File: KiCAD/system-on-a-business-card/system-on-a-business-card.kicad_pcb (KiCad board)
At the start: 2 copper layers, 85 x 54 mm, 92 parts, among them J1 USB_C_Receptacle, J2 X077-6428TSWCG01-H13, J3 Conn_01x04_Socket, J4 TF-018B-H15, Q1 2N7002K, Q2 2N7002K, SW1 SW_Push, SW2 SW_Push, U1 USBLC6-2SC6, U2 ESP32-C3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

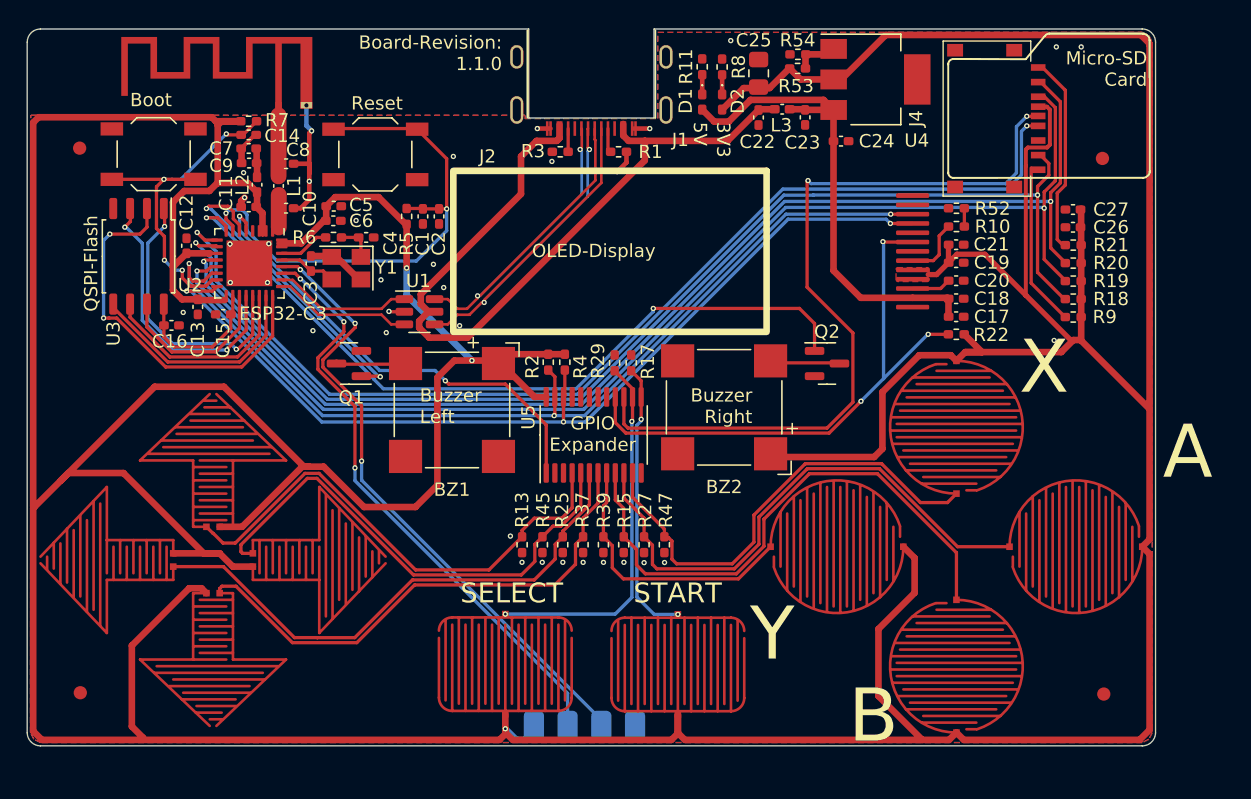
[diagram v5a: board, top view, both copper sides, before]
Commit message: #10: created version with DAC, Op Amp and speaker
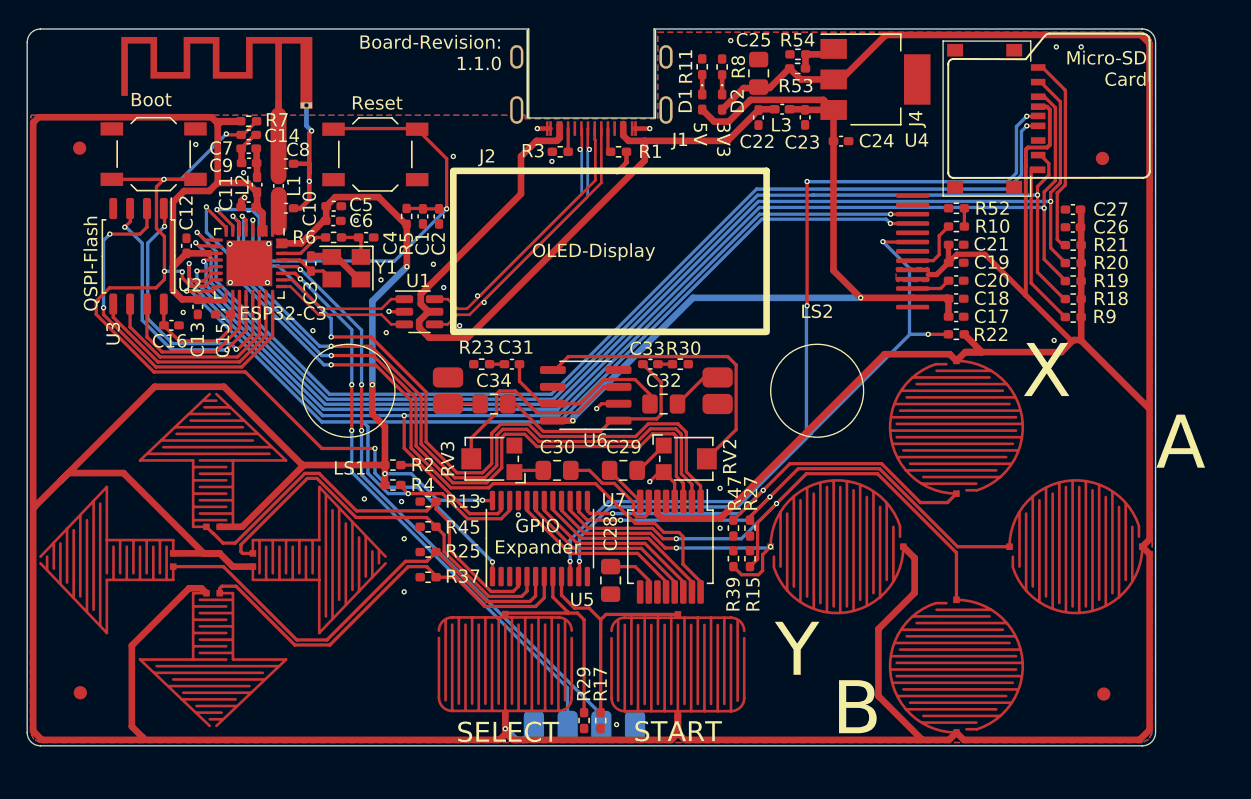
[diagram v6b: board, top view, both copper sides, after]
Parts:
- removed BZ1, BZ2: MLT-7525, Buzzer_Beeper:MagneticBuzzer_CUI_CMT-8504-100-SMT
- removed Q1, Q2: 2N7002K, Package_TO_SOT_SMD:SOT-23
- added C28: 10u, Capacitor_SMD:C_0805_2012Metric_Pad1.18x1.45mm_HandSolder, F.Cu at (121.5, 111.5)
- added C29: 10u, Capacitor_SMD:C_0805_2012Metric_Pad1.18x1.45mm_HandSolder, F.Cu at (122.4, 103.2)
- added C30: 10u, Capacitor_SMD:C_0805_2012Metric_Pad1.18x1.45mm_HandSolder, F.Cu at (117.4, 103.2)
- added C31: 50n, Capacitor_SMD:C_0402_1005Metric_Pad0.74x0.62mm_HandSolder, F.Cu at (114.0, 95.2)
- added C32: 250u, Capacitor_SMD:C_0805_2012Metric_Pad1.18x1.45mm_HandSolder, F.Cu at (125.5, 98.2)
- added C33: 50n, Capacitor_SMD:C_0402_1005Metric_Pad0.74x0.62mm_HandSolder, F.Cu at (124.5, 95.2)
- added C34: 250u, Capacitor_SMD:C_0805_2012Metric_Pad1.18x1.45mm_HandSolder, F.Cu at (112.7, 98.2)
- added LS1: Speaker_Left, Prj_speaker:Radial_10mm, F.Cu at (101.7, 97.2)
- added LS2: Speaker_Right, Prj_speaker:Radial_10mm, F.Cu at (137.0, 97.2)
- added R23: 10R, Resistor_SMD:R_0402_1005Metric_Pad0.72x0.64mm_HandSolder, F.Cu at (111.7, 95.2)
- added R30: 10R, Resistor_SMD:R_0402_1005Metric_Pad0.72x0.64mm_HandSolder, F.Cu at (126.7, 95.2)
- added RV2: 10k, Potentiometer_SMD:Potentiometer_Bourns_TC33X_Vertical, F.Cu at (127.2, 102.4)
- added RV3: 10k, Potentiometer_SMD:Potentiometer_Bourns_TC33X_Vertical, F.Cu at (112.4, 102.4)
- added U6: RC4580, Package_SO:SOIC-8_3.9x4.9mm_P1.27mm, F.Cu at (119.6, 97.6)
- added U7: PCM1754, Package_SO:SSOP-16_5.3x6.2mm_P0.65mm, F.Cu at (126.0, 109.0)
- moved R17 27.0 mm to (120.7, 122.1), turned to -90 degrees
- moved R29 27.0 mm to (119.5, 122.1), turned to -90 degrees
- moved R4 15.9 mm to (105.0, 104.3), turned to 0 degrees
- moved R2 14.0 mm to (105.0, 102.8), turned to 0 degrees
- moved R37 11.9 mm to (107.7, 111.3), turned to 180 degrees
- moved R25 10.2 mm to (107.7, 109.4), turned to 180 degrees
- moved R39 9.85 mm to (130.7, 109.9), turned to 90 degrees
- moved R15 9.57 mm to (131.9, 109.9), turned to 90 degrees
- moved U5 8.79 mm to (116.1, 108.4)
- moved R45 8.72 mm to (107.7, 107.5), turned to 180 degrees
- moved R27 8.08 mm to (131.9, 107.6)
- moved R13 7.79 mm to (107.7, 105.6), turned to 180 degrees
- moved R47 5.35 mm to (130.7, 107.6)
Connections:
- U2 pad 4: unconnected-(U2-XTAL_32K_P/ADC1_CH0-Pad4) -> /Audio Circuit/BCLK
- U2 pad 5: /Host/IO_EXP_INT -> /Audio Circuit/SERIAL_DATA
- U2 pad 6: BUZZER_L -> /Audio Circuit/LRCLK
- U2 pad 8: BUZZER_R -> /Audio Circuit/SCLK
- U5 pad 1: /Host/IO_EXP_INT -> BOOT
- U5 pad 10: A -> /Resistive Touch Circuit/SDCard_DET
- U5 pad 11: X -> RESET_DISPLAY
- U5 pad 13: START -> X
- U5 pad 14: SELECT -> A
- U5 pad 15: /Resistive Touch Circuit/SDCard_DET -> B
- U5 pad 16: RESET_DISPLAY -> Y
- U5 pad 17: unconnected-(U5-P14-Pad17) -> /Audio Circuit/FMT
- U5 pad 18: unconnected-(U5-P15-Pad18) -> /Audio Circuit/MUTE
- U5 pad 19: unconnected-(U5-P16-Pad19) -> /Audio Circuit/DEMP
- U5 pad 20: unconnected-(U5-P17-Pad20) -> /Audio Circuit/TEST
- U5 pad 8: Y -> SELECT
- U5 pad 9: B -> START
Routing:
- net BUZZER_R: track 58.2 -> 0.00 mm, vias 2 -> 0
- net /Audio Circuit/SCLK: track 0.00 -> 57.5 mm, vias 0 -> 2
- net /Audio Circuit/LRCLK: track 0.00 -> 56.2 mm, vias 0 -> 2
- net /Audio Circuit/SERIAL_DATA: track 0.00 -> 56.1 mm, vias 0 -> 2
- net /Audio Circuit/BCLK: track 0.00 -> 55.5 mm, vias 0 -> 2
- net BOOT: track 26.9 -> 74.5 mm, vias 4 -> 6
- net /Host/IO_EXP_INT: track 35.2 -> 0.00 mm, vias 2 -> 0
- net +5V: track 37.5 -> 64.5 mm, vias 0 -> 2
- net BUZZER_L: track 23.5 -> 0.00 mm, vias 2 -> 0
- net Net-(U6B-+): track 0.00 -> 22.3 mm
- net Net-(C33-Pad1): track 0.00 -> 17.3 mm
- net Net-(U6A-+): track 0.00 -> 16.2 mm
- net /Audio Circuit/DEMP: track 0.00 -> 14.2 mm
- net /Audio Circuit/TEST: track 0.00 -> 14.2 mm
- net /Audio Circuit/MUTE: track 0.00 -> 14.2 mm
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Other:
- board text removed: "Buzzer Left"
- board text removed: "Buzzer Right"
